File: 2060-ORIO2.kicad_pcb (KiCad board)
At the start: 2 copper layers, 100 x 100 mm, 185 parts, among them J11 RaspberryPI-B+header, J12 Conn_01x04, J13 Conn_01x08, J14 Conn_01x08, J15 Conn_01x08, J16 Conn_01x10, J17 Conn_01x10, J18 Conn_01x10, J19 Conn_01x10, J20 Conn_01x09, J21 Conn_01x08, J22 Conn_01x08, J23 Conn_01x08, J24 Conn_01x08, J25 Conn_01x08, J26 Conn_01x08, J27 Conn_01x02, J28 Conn_01x16, J29 Conn_01x16, J30 Conn_01x16, J31 Conn_01x08, J32 Conn_01x08, J33 Conn_01x08, J34 Conn_01x08, J35 TBL001-500-02GY-2GY, Q11 ULN2803ADWR, SW11 SW_DIP_x08, U11 ICE40HX4K-TQ144, U12 SN74LVC4245AN, U13 SN74LVC4245AN, U14 SN74LVC4245AN, U15 TPS563231, U16 MCP3008, U17 AZ1117CH-3.3TRG1, U18 AZ1117CH-3.3TRG1, U19 AZ1117CH-1.2, U20 TPS563231, U21 SN74LVC4245AN, U22 SN74LVC4245AN, U23 SN74LVC4245AN, U24 SN74LVC4245AN, U25 TPS563231, U26 AP3012, Y11 XLH536025_000000I

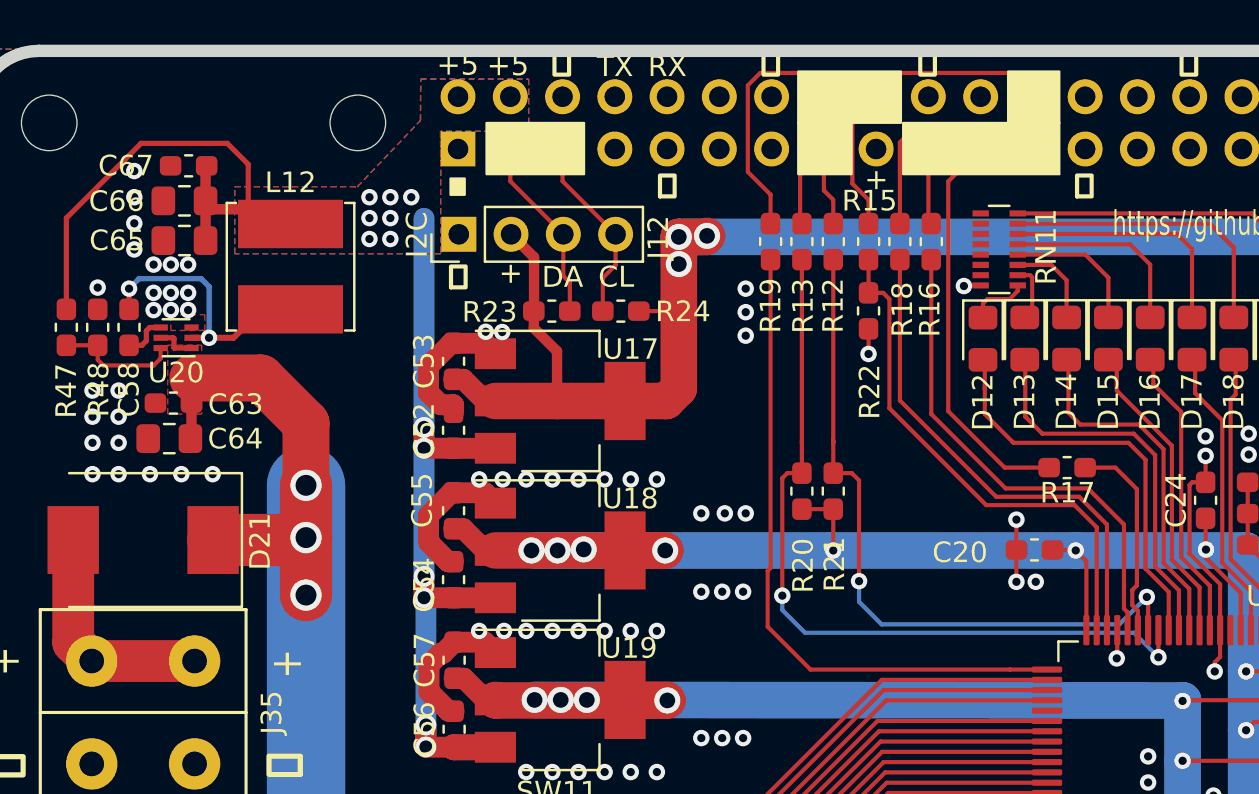
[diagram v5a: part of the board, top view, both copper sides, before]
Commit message: Added power LED & GND plane vias.
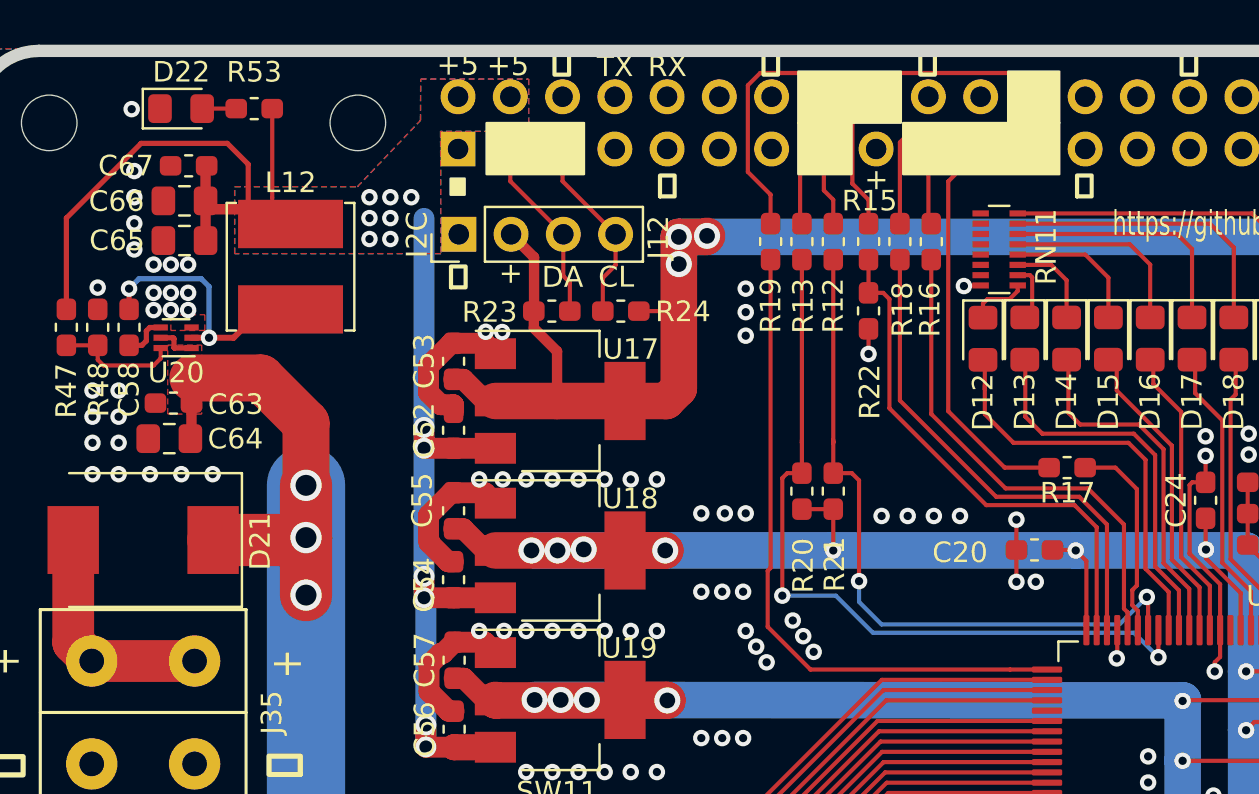
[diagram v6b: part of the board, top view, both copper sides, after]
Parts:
- added D22: LED_ALT, LED_SMD:LED_0805_2012Metric_Pad1.15x1.40mm_HandSolder, F.Cu at (81.9, 44.8)
- added LOGO11: Logo_Open_Hardware_Small, Symbol:OSHW-Logo_11.4x12mm_SilkScreen, B.Cu at (125.6, 58.3)
- added R53: 1K, Resistor_SMD:R_0603_1608Metric_Pad1.05x0.95mm_HandSolder, F.Cu at (85.5, 44.8)
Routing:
- net 5V_PI: track 66.9 -> 73.1 mm
- net Net-(D22-Pad2): track 0.00 -> 1.66 mm
- net GND: vias 292 -> 303

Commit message: Fuses, 4-layer, RSL, 86 the Solenoid GND,
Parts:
- added F11: .5A, Fuse:Fuse_2920_7451Metric_Pad2.10x5.45mm_HandSolder, F.Cu at (90.1, 72.2)
- added F12: Polyfuse, Fuse:Fuse_2920_7451Metric_Pad2.10x5.45mm_HandSolder, F.Cu at (90.1, 65.7)
- added Q12: BCV27, Package_TO_SOT_SMD:SOT-23, F.Cu at (86.6, 98.5)
- added R54: 1K, Resistor_SMD:R_0603_1608Metric_Pad1.05x0.95mm_HandSolder, F.Cu at (90.1, 99.5)
- J14: value Conn_01x08 -> Conn_01x02; footprint Connector_PinHeader_2.54mm:PinHeader_1x08_P2.54mm_Vertical -> Connector_PinHeader_2.54mm:PinHeader_1x02_P2.54mm_Vertical
- moved J14 7.03 mm to (82.7, 96.0)
- moved U19 3.07 mm to (103.4, 73.5)
- moved C52 3.05 mm to (98.2, 60.4)
- moved C53 3.05 mm to (98.2, 57.1)
- moved C54 3.05 mm to (98.2, 67.7)
- moved C55 3.05 mm to (98.2, 64.4)
- moved C56 3.05 mm to (98.2, 75.0)
- moved C57 3.05 mm to (98.2, 71.6)
- moved U17 3.05 mm to (103.4, 59.0)
- moved U18 3.05 mm to (103.4, 66.3)
- moved Q11 2.51 mm to (86.9, 108.5)
- moved J13 2.49 mm to (75.7, 96.0)
- moved J15 2.47 mm to (78.3, 96.0)
- moved R23 1.14 mm to (99.9, 53.5)
- moved R24 1.14 mm to (103.3, 53.5)
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- renumbered LOGO11 to ?
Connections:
- net VCC_SOL renamed VCC_SOL_24
- C78 pad 1: +BATT -> VCC_SOL_12
- D21 pad 1: +BATT -> Net-(D21-Pad1)
- J14 pad 1: GND -> VCC_SOL_12
- J14 pad 2: GND -> Net-(J14-Pad2)
- L14 pad 1: +BATT -> VCC_SOL_12
- U11 pad 128: Net-(U11-Pad128) -> /FPGA_RSL
- U26 pad 4: +BATT -> VCC_SOL_12
- U26 pad 5: +BATT -> VCC_SOL_12
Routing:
- net +3V3: track 357.3 -> 162.5 mm, vias 22 -> 23
- net /FPGA_RSL: track 0.00 -> 55.5 mm, vias 0 -> 2
- net VCC_SOL_12: track 0.00 -> 33.2 mm
- net +BATT: track 173.9 -> 157.4 mm
- net GND: track 136.6 -> 130.4 mm, vias 303 -> 201
- net /SOL_0: track 49.6 -> 53.1 mm
- net Net-(J14-Pad2): track 0.00 -> 2.89 mm
- net Net-(D21-Pad1): track 0.00 -> 2.62 mm
- net /SOL_7: track 48.1 -> 50.6 mm
- net /SOL_6: track 48.4 -> 50.9 mm
- net /SOL_5: track 48.7 -> 51.2 mm
- net /SOL_4: track 49.3 -> 51.8 mm
- net /SOL_3: track 49.7 -> 52.2 mm
- net /SOL_2: track 49.8 -> 52.3 mm
- net /SOL_1: track 49.7 -> 52.2 mm
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- added copper zone on In2.Cu, net +3V3
- added copper zone on In1.Cu, net GND
- added copper zone on In2.Cu, net GND
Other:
- copper layers 2 -> 4
- board text added: "RSL"
- board text added: "SCL"
- board text added: "SDA"
- board text removed: "CL"
- board text removed: "DA"

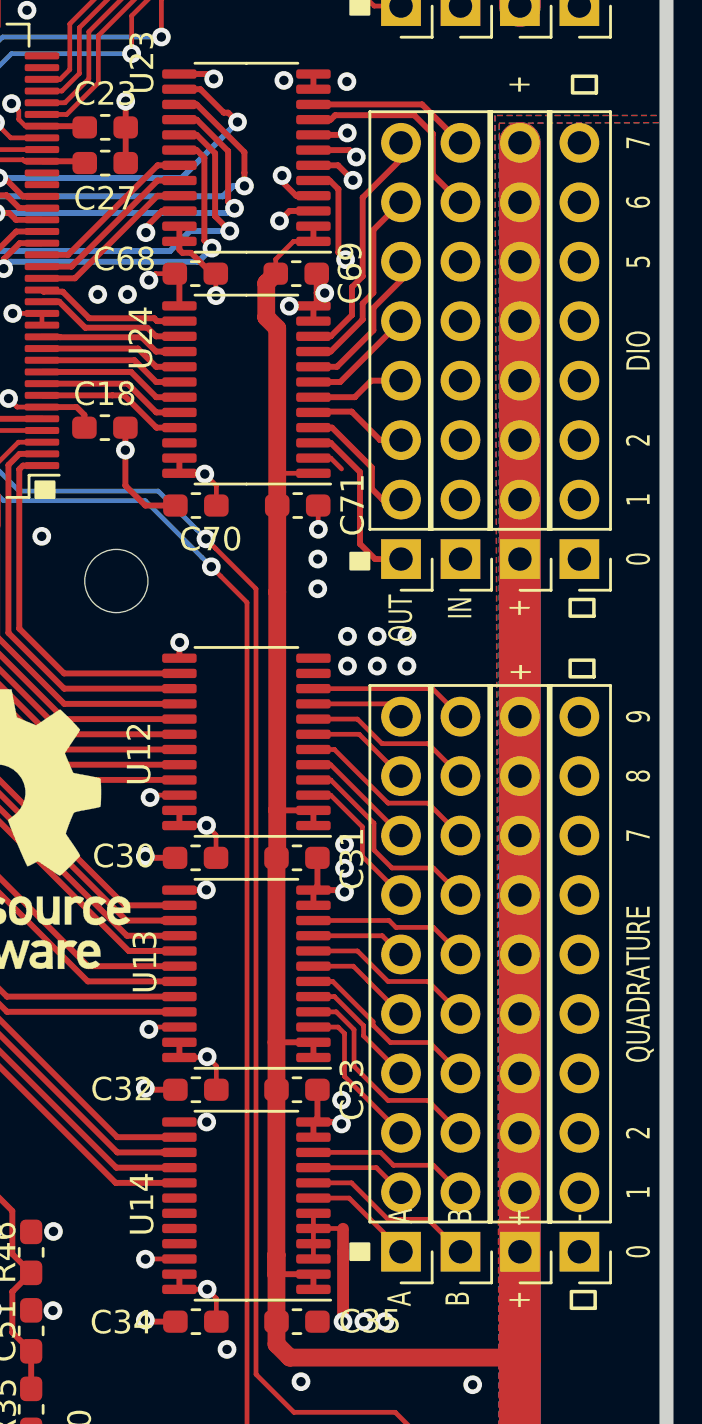
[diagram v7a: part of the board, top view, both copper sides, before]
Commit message: Added pul;lup resistors on DIN level shifters.
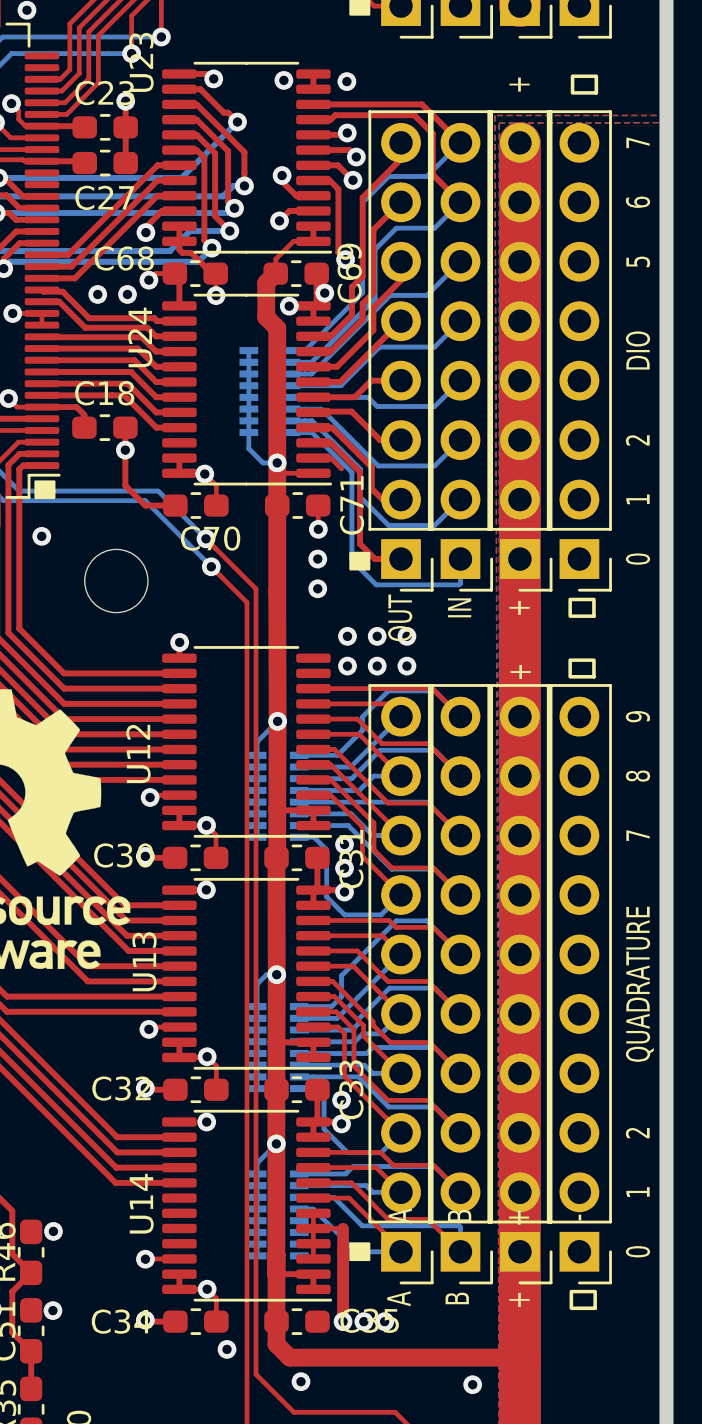
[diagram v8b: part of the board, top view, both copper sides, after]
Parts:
- added RN1: 10K, Resistor_SMD:R_Array_Convex_8x0602, B.Cu at (155.4, 103.7)
- added RN2: 10K, Resistor_SMD:R_Array_Convex_8x0602, B.Cu at (155.4, 114.4)
- added RN3: 10K, Resistor_SMD:R_Array_Convex_8x0602, B.Cu at (155.4, 121.6)
- added RN4: 10K, Resistor_SMD:R_Array_Convex_8x0602, B.Cu at (155.1, 86.4)
- gave numbers to parts that had none: 1
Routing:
- net VCC_IO: track 346.8 -> 368.4 mm, vias 0 -> 4
- net /DIN0: track 20.2 -> 33.5 mm
- net /DIN7: track 6.96 -> 20.1 mm
- net /DIN6: track 8.92 -> 20.2 mm
- net /DIN1: track 19.4 -> 29.7 mm
- net /QB5: track 6.88 -> 16.4 mm
- net /DIN5: track 9.87 -> 19.1 mm
- net /QB9: track 6.78 -> 15.6 mm
- net /DIN2: track 15.1 -> 23.8 mm
- net /QB0: track 7.50 -> 16.0 mm
- net /DIN4: track 11.5 -> 19.9 mm
- net /QB4: track 7.40 -> 15.6 mm
- net /QB6: track 9.76 -> 17.9 mm
- net /QB2: track 10.1 -> 18.0 mm
- net /DIN3: track 13.0 -> 20.8 mm
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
